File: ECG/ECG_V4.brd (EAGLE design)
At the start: 62.2 x 34.3 mm, 35 parts, among them U1 AD8232, U3 BGM111-VISUAL-A

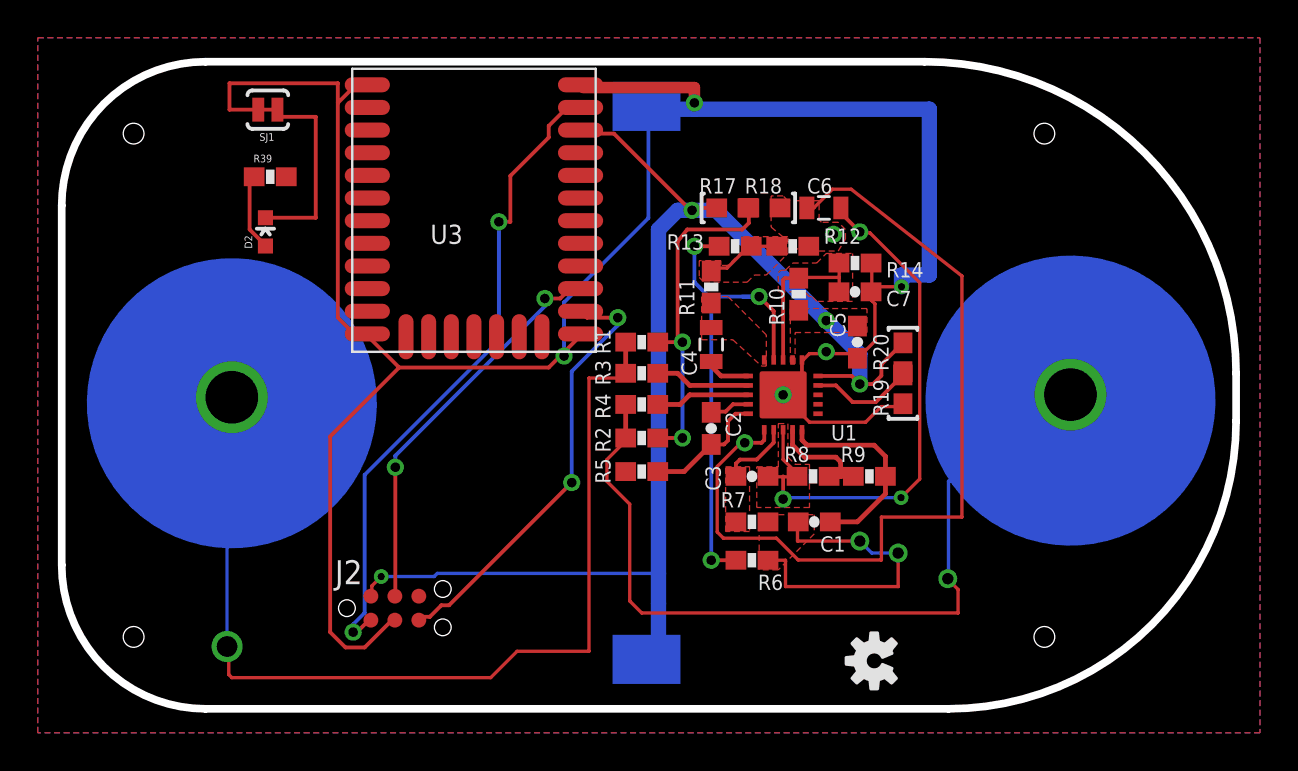
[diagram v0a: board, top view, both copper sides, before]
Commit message: Connections Debugged
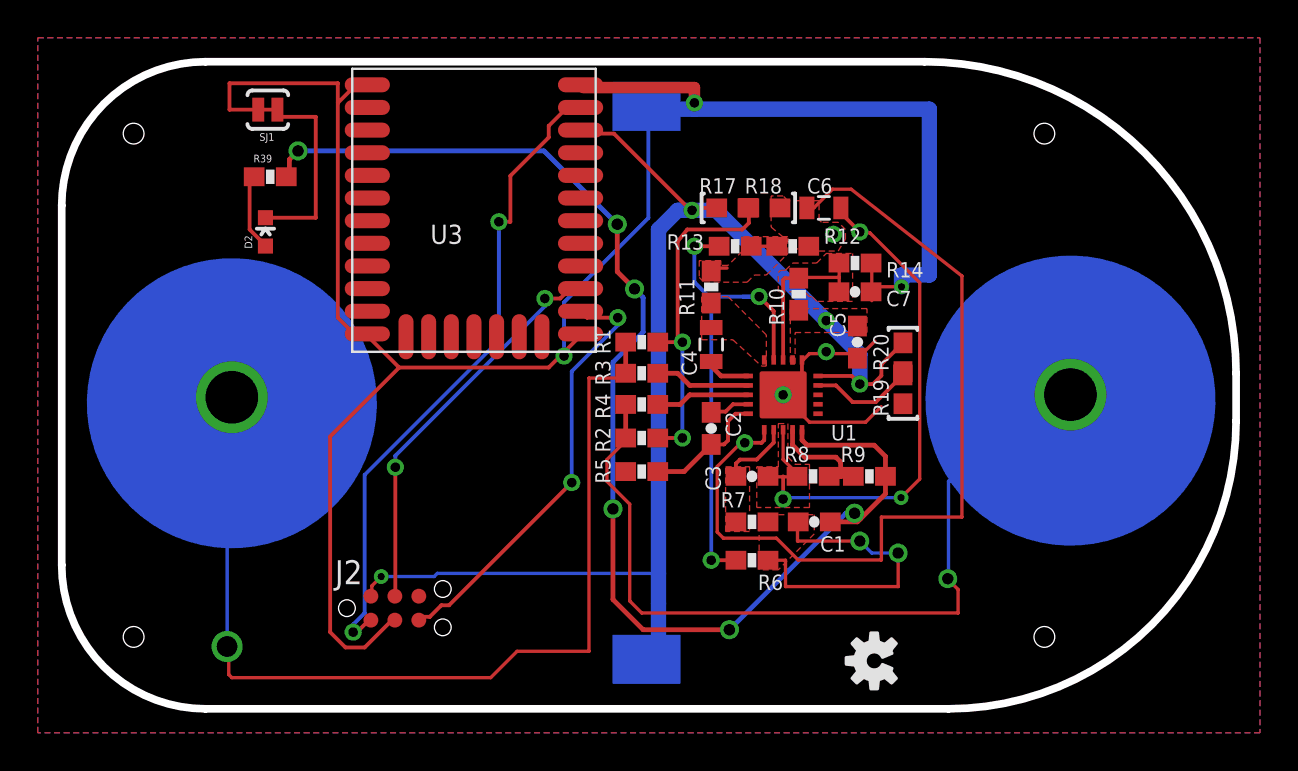
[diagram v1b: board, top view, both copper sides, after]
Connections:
- removed net N$38: R39.2
- net SIGNAL_OUT: now also R39.2
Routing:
- net SIGNAL_OUT: track 10.8 -> 68.7 mm, vias 0 -> 6
- net GND: track 127.3 -> 124.0 mm
- net N$14: track 4.10 -> 2.47 mm
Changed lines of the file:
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@@
 <autorouter>
 <pass name="Default">
-<param name="RoutingGrid" value="50mil"/>
+<param name="RoutingGrid" value="6.25mil"/>
 <param name="AutoGrid" value="1"/>
 <param name="Efforts" value="2"/>
 <param name="TopRouterVariant" value="1"/>
 <param name="tpViaShape" value="round"/>
-<param name="PrefDir.1" value="a"/>
+<param name="PrefDir.1" value="*"/>
 <param name="PrefDir.2" value="0"/>
 <param name="PrefDir.3" value="0"/>
@@
 <param name="PrefDir.14" value="0"/>
 <param name="PrefDir.15" value="0"/>
-<param name="PrefDir.16" value="a"/>
+<param name="PrefDir.16" value="-"/>
 <param name="cfVia" value="8"/>
 <param name="cfNonPref" value="5"/>
@@
 <wire x1="45.6946" y1="34.0614" x2="45.593" y2="34.163" width="0.1778" layer="1"/>
 <wire x1="47.1805" y1="33.8963" x2="47.244" y2="33.821" width="0.1778" layer="1"/>
-<wire x1="48.5013" y1="31.2547" x2="49.657" y2="31.2547" width="0.1778" layer="1"/>
 <wire x1="47.6758" y1="30.4292" x2="48.5013" y2="31.2547" width="0.1778" layer="1"/>
 <wire x1="44.704" y1="30.4292" x2="47.6758" y2="30.4292" width="0.1778" layer="1"/>
@@
 <wire x1="43.3832" y1="31.75" x2="43.307" y2="31.877" width="0.1778" layer="1"/>
 <wire x1="48.006" y1="36.8681" x2="48.006" y2="37.1983" width="0.1778" layer="1"/>
-<wire x1="48.1711" y1="36.703" x2="48.006" y2="36.8681" width="0.1778" layer="1"/>
-<wire x1="48.1711" y1="34.7218" x2="48.1711" y2="36.703" width="0.1778" layer="1"/>
 <wire x1="47.3456" y1="33.8963" x2="48.1711" y2="34.7218" width="0.1778" layer="1"/>
 <wire x1="48.006" y1="37.1983" x2="47.967" y2="37.338" width="0.1778" layer="1"/>
@@
 <wire x1="48.729" y1="27.559" x2="48.729" y2="28.614" width="0.254" layer="1"/>
 <wire x1="45.808" y1="25.146" x2="47.244" y2="25.146" width="0.254" layer="1"/>
-<wire x1="47.244" y1="25.146" x2="48.729" y2="26.631" width="0.254" layer="1"/>
+<wire x1="47.244" y1="25.146" x2="47.3964" y2="25.2984" width="0.254" layer="1"/>
+<wire x1="47.3964" y1="25.2984" x2="48.729" y2="26.631" width="0.254" layer="1"/>
 <wire x1="48.729" y1="27.559" x2="48.729" y2="26.631" width="0.254" layer="1"/>
+<contactref element="R39" pad="2"/>
+<wire x1="17.145" y1="44.3484" x2="17.145" y2="43.434" width="0.254" layer="1"/>
+<wire x1="17.6022" y1="44.8056" x2="17.145" y2="44.3484" width="0.254" layer="1"/>
+<wire x1="30.6324" y1="44.8056" x2="17.6022" y2="44.8056" width="0.254" layer="16"/>
+<wire x1="34.5186" y1="40.9194" x2="30.6324" y2="44.8056" width="0.254" layer="16"/>
+<wire x1="34.5186" y1="38.4048" x2="34.5186" y2="40.9194" width="0.254" layer="1"/>
+<wire x1="35.433" y1="37.4904" x2="34.5186" y2="38.4048" width="0.254" layer="1"/>
+<wire x1="35.8902" y1="37.0332" x2="35.433" y2="37.4904" width="0.254" layer="16"/>
+<wire x1="35.8902" y1="35.2044" x2="35.8902" y2="37.0332" width="0.254" layer="16"/>
+<wire x1="34.29" y1="33.6042" x2="35.8902" y2="35.2044" width="0.254" layer="16"/>
+<wire x1="34.29" y1="25.8318" x2="34.29" y2="33.6042" width="0.254" layer="16"/>
+<wire x1="34.29" y1="21.0312" x2="34.29" y2="25.8318" width="0.254" layer="1"/>
+<wire x1="35.8902" y1="19.431" x2="34.29" y2="21.0312" width="0.254" layer="1"/>
+<wire x1="40.4622" y1="19.431" x2="35.8902" y2="19.431" width="0.254" layer="1"/>
+<wire x1="46.6344" y1="25.6032" x2="40.4622" y2="19.431" width="0.254" layer="16"/>
+<wire x1="47.0916" y1="25.6032" x2="46.6344" y2="25.6032" width="0.254" layer="16"/>
+<wire x1="47.3964" y1="25.2984" x2="47.0916" y2="25.6032" width="0.254" layer="1"/>
+<wire x1="17.145" y1="43.434" x2="16.979" y2="43.434" width="0.254" layer="1"/>
+<via x="17.6022" y="44.8056" extent="1-16" drill="0.6096"/>
+<via x="34.5186" y="40.9194" extent="1-16" drill="0.6096"/>
+<via x="35.433" y="37.4904" extent="1-16" drill="0.6096"/>
+<via x="34.29" y="25.8318" extent="1-16" drill="0.6096"/>
+<via x="40.4622" y="19.431" extent="1-16" drill="0.6096"/>
+<via x="47.0916" y="25.6032" extent="1-16" drill="0.6096"/>
 </signal>
 <signal name="REFOUT">
@@
 <wire x1="42.9768" y1="39.751" x2="42.965" y2="39.751" width="0.1778" layer="1"/>
 <wire x1="40.3352" y1="38.5953" x2="39.5097" y2="38.5953" width="0.1778" layer="1"/>
-<wire x1="41.4909" y1="39.751" x2="40.3352" y2="38.5953" width="0.1778" layer="1"/>
 <wire x1="39.5097" y1="38.5953" x2="39.497" y2="38.442" width="0.1778" layer="1"/>
 <wire x1="41.4909" y1="39.751" x2="41.617" y2="39.751" width="0.1778" layer="1"/>
@@
 <wire x1="16.51" y1="46.609" x2="16.51" y2="46.99" width="0.2032" layer="1"/>
 </signal>
-<signal name="N$38">
-<contactref element="R39" pad="2"/>
-</signal>
 </signals>
